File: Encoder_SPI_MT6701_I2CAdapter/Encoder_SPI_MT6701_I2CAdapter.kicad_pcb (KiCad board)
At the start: 2 copper layers, 21 x 17 mm, 21 parts, among them J1 3.3V in, J2 JST_SH_SM04B, J3 5V in, J4 Conn_01x06_MountingPin, U1 NXB0102GTX

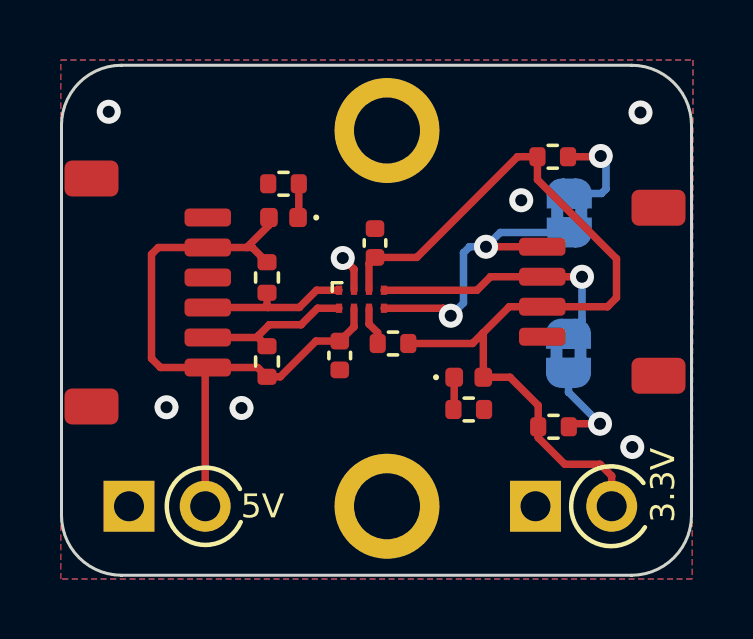
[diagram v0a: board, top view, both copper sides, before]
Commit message: fix incorrect footprint
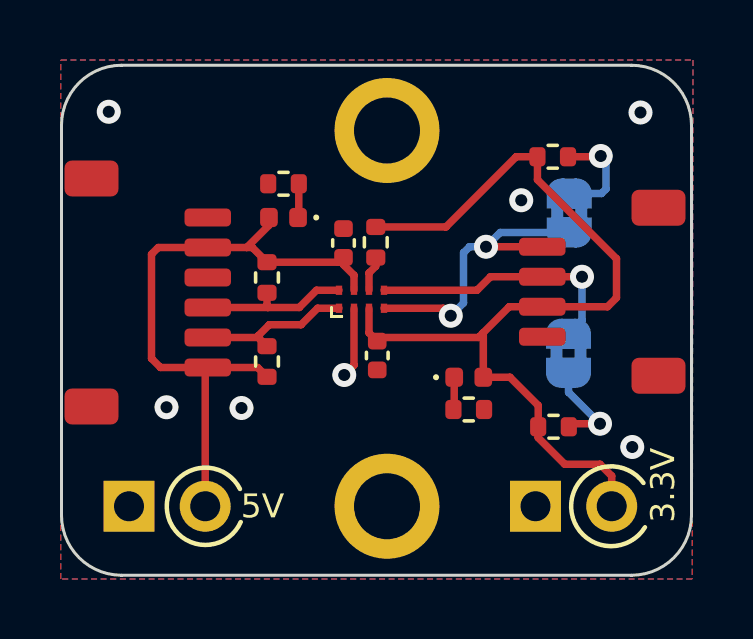
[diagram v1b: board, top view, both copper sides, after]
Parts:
- J4: value Conn_01x06_MountingPin -> JST_SH_SM06B
- R4: value 4k7 -> 2k2
- moved C2 3.75 mm to (78.5, 39.5), turned to -90 degrees
- moved C1 3.75 mm to (79.6, 43.2), turned to 90 degrees
- moved R4 3.42 mm to (79.6, 39.5), turned to -90 degrees
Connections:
- U1 pad 1: /MISO -> /SCK
- U1 pad 4: /SDA_A -> /SCL_A
- U1 pad 5: /SCL_A -> /SDA_A
- U1 pad 8: /SCK -> /MISO
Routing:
- net GND: track 1.23 -> 2.36 mm
- net VDD: track 30.1 -> 30.7 mm
